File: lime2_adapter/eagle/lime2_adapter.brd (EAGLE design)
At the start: 23 parts, among them T1 MOSFET-N-NX7002AK, T2 MOSFET-N-NX7002AK, X1 lcd0_d02, X2 D-SUB15-HDR15RA, X4 XF2-40-RARBT, X5 FPC40-525594052

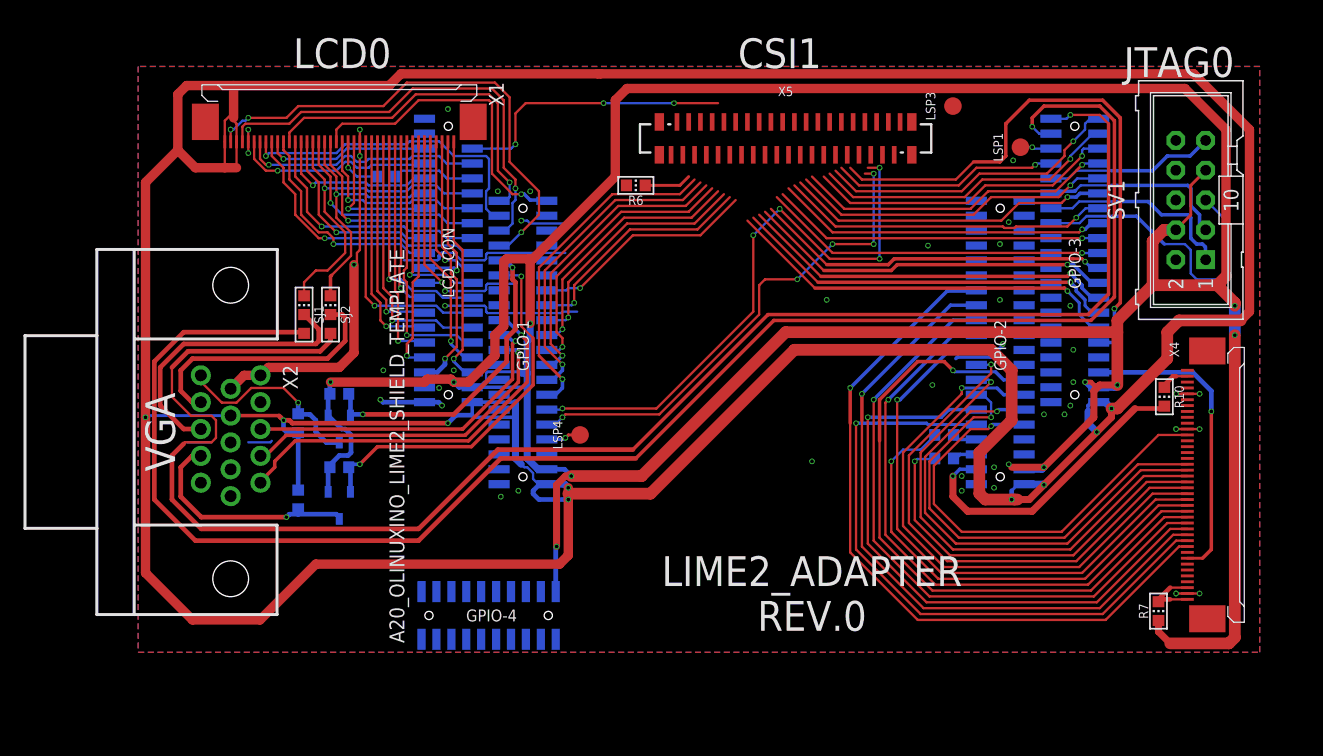
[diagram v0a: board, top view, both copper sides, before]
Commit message: Realize ECOs from Luc 190508
- Change X1-02 (X1B) to be disconnected
- Change X1-04 (X1D) to be disconnected
- Change X1-06 (X1F) to be disconnected
- Change X1-07 (X1G) to GPIO1-38(PC24)
- Change X1-08 (X1H) to GPIO1-40(PC23)
- Change X1-12 (X1L) to be disconnected
- Change X1-20 (X1T) to be disconnected
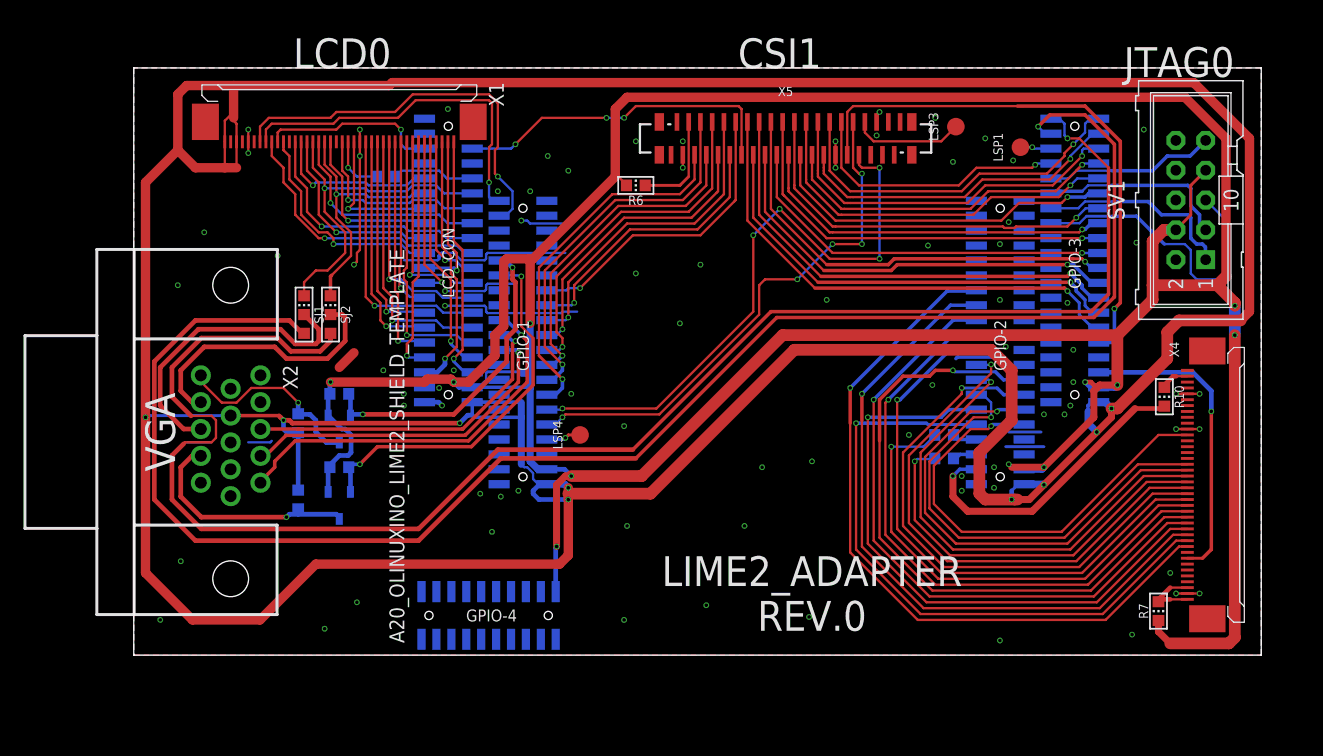
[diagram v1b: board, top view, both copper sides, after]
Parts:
- X1: value lcd0_d02 -> LCD
- moved LSP3 1.77 mm to (71.0, 51.0)
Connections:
- net EINT15/NCE7/SPI2_MISO/PC22: no longer X1.20
- net NC/IR0_RX/PB4: no longer X1.6
- net NC/IR0_TX/SPDIF_MCLK/STANBYWFI/PB3: no longer X1.7
- net NDQS/PC24: now also X1.7; no longer X1.8
- net SPI0_CS0/PC23: now also X1.8; no longer X1.12
- net TWI1_SCK/PB18: no longer X1.4
- net TWI1_SDA/PB19: no longer X1.2
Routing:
- net TWI1_SDA/PB19: track 42.5 -> 0.00 mm, vias 3 -> 0
- net TWI1_SCK/PB18: track 37.7 -> 0.00 mm, vias 1 -> 0
- net EINT15/NCE7/SPI2_MISO/PC22: track 27.1 -> 0.00 mm, vias 1 -> 0
- net NC/IR0_TX/SPDIF_MCLK/STANBYWFI/PB3: track 20.7 -> 0.00 mm, vias 1 -> 0
- net NC/IR0_RX/PB4: track 17.0 -> 0.00 mm, vias 1 -> 0
- net GND: track 90.0 -> 77.9 mm, vias 43 -> 82
- net DISPEN: track 0.00 -> 9.48 mm
- net CSI1_D9/PH9: track 34.3 -> 42.7 mm
- net CSI1_D11/PH11: track 32.2 -> 40.1 mm
- net CSI1_D13/PH13: track 30.4 -> 37.8 mm
- net NDQS/PC24: track 27.0 -> 34.1 mm
- net CSI1_D7/PG11: track 19.3 -> 25.9 mm
- net CSI1_D5/PG9: track 21.3 -> 27.4 mm
- net CSI1_D15/PH15: track 28.5 -> 34.6 mm
- net CSI1_D3/PG7: track 24.0 -> 29.7 mm
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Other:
- board outline added: 96 x 50 mm

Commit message: lime2_adapter
- Change VCC_CSI0 (Camera) from X4-2 to X4-3
- Connect X1-2 to GND.
- Provide access to TVOUT3, LINEIN[L|R] and FMIN[L|R]
- Provide access to MIC[1|2]
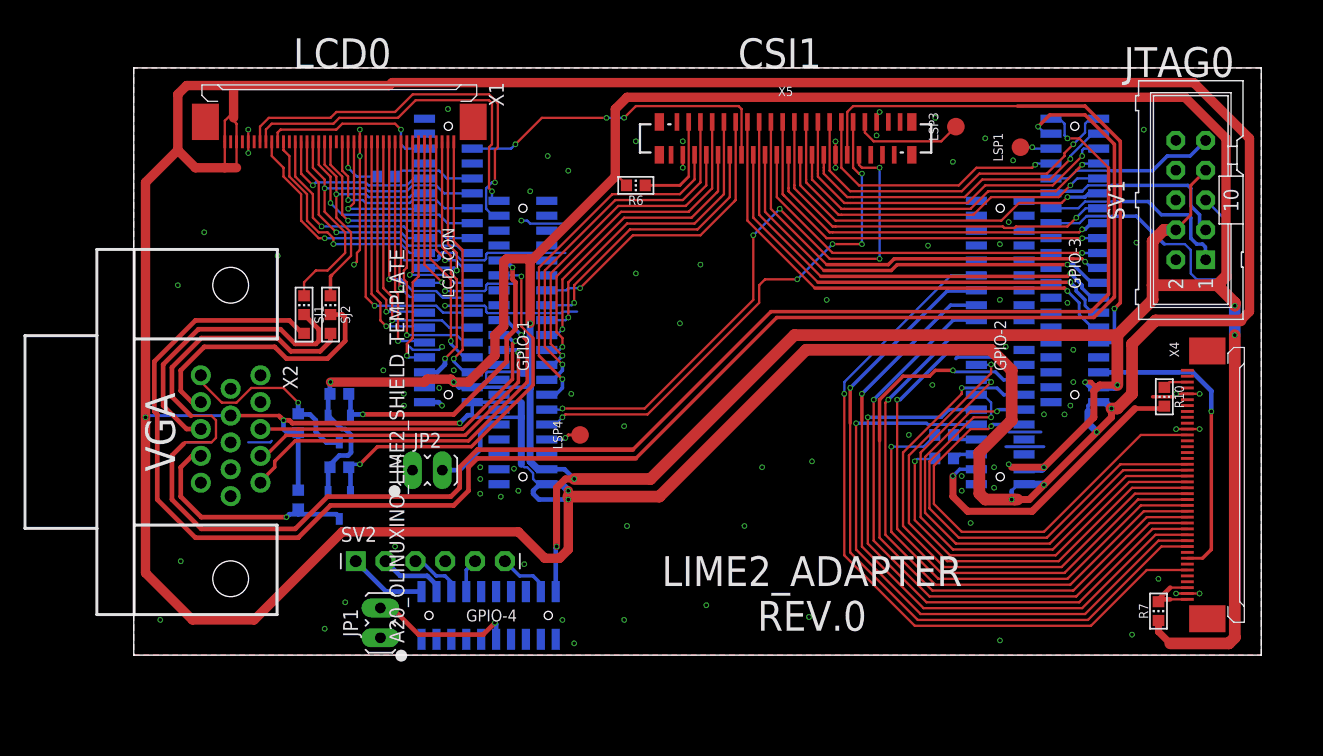
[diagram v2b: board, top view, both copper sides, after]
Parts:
- added JP1, JP2: JP1E, jumper:JP1
- added SV2: (no value), con-lstb:MA06-1
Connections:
- removed net CSI0_IO0: X4.35
- removed net GNDA: A20_OLINUXINO_LIME2_SHIELD.1-4
- removed net N$24: X4.16
- removed net N$25: X4.15
- removed net N$26: X4.14
- removed net N$27: X4.13
- removed net N$30: X4.10
- removed net N$31: X4.9
- removed net N$32: X4.8
- removed net N$33: X4.7
- removed net N$34: X4.6
- removed net N$36: X4.4
- removed net N$37: X4.3
- removed net N$39: X4.1
- removed net N$4: X4.36
- removed net N$6: X4.34
- removed net N$7: R10.1, X4.2
- removed net N$8: X4.32
- net FMINL: now also SV2.1
- net FMINR: now also SV2.2
- net GND: now also A20_OLINUXINO_LIME2_SHIELD.1-4, JP1.1, JP2.1, SV2.4
- net HSDA/UART7_RX/PS2_SDA0/PI21: now also X4.35
- net LINEINL: now also SV2.3
- net LINEINR: now also SV2.5
- net MICIN1: now also JP2.2
- net MICIN2: now also JP1.2
- net N$3: now also R10.1, X4.3; no longer X4.37
- net TVOUT3: now also SV2.6
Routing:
- net HSDA/UART7_RX/PS2_SDA0/PI21: track 0.00 -> 63.4 mm, vias 0 -> 1
- net MICIN2: track 0.00 -> 12.5 mm, vias 0 -> 1
- net MICIN1: track 0.00 -> 7.32 mm
- net FMINL: track 0.00 -> 6.67 mm
- net FMINR: track 0.00 -> 5.74 mm
- net LINEINL: track 0.00 -> 4.60 mm
- net TVOUT3: track 0.00 -> 4.53 mm
- net GND: track 77.9 -> 81.2 mm, vias 82 -> 89
- net LINEINR: track 0.00 -> 2.90 mm
- net +5V: track 369.4 -> 372.1 mm
- net N$7: track 2.47 -> 0.00 mm
- net N$3: track 0.00 -> 2.15 mm
- net LCD1_VSYNC/PH27: track 139.8 -> 140.8 mm
- net LCD1_HSYNC/PH26: track 141.1 -> 141.9 mm
- net CSI1_VSYNC/PG3: track 51.4 -> 50.8 mm
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
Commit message: lime2_adapter: Move LCD connector left to avoid collision with USB/ETH.
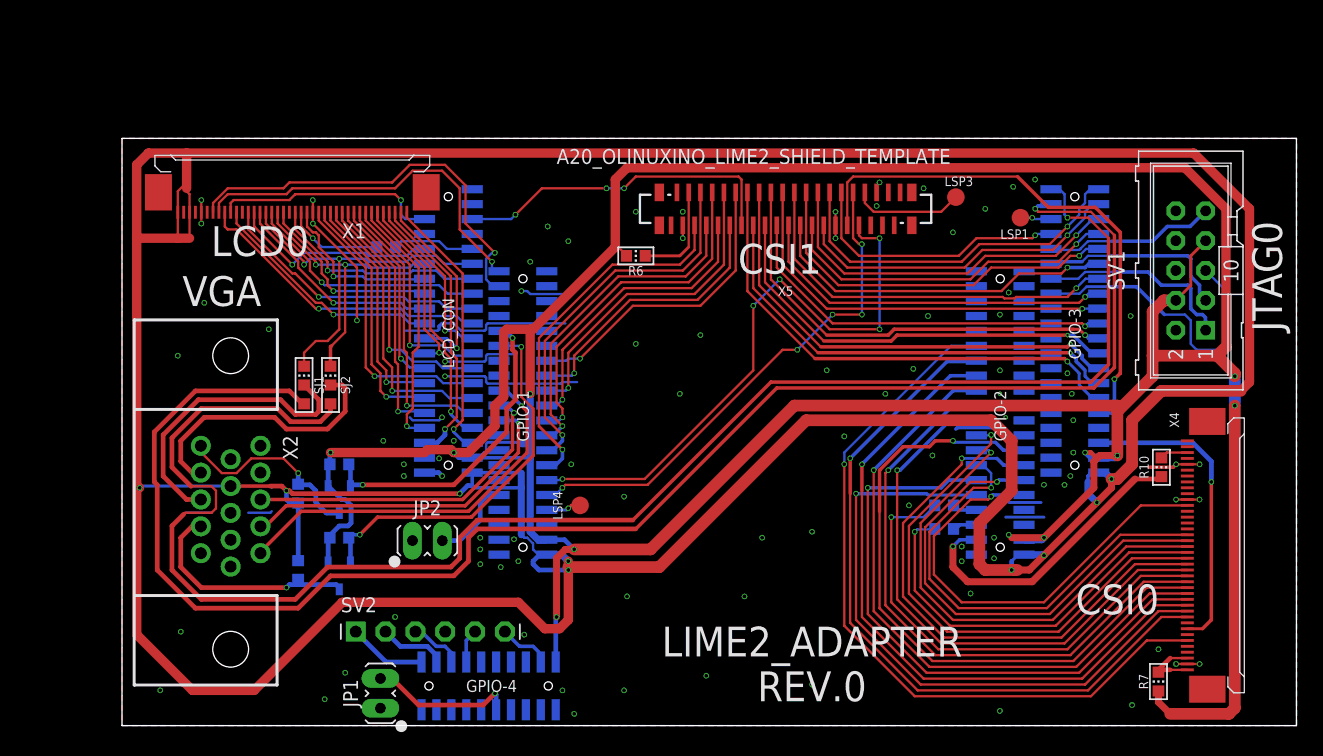
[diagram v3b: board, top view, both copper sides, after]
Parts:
- moved X1 7.21 mm to (14.5, 46.2)
- moved R10 6.01 mm to (88.5, 22.0)
- moved A20_OLINUXINO_LIME2_SHIELD 6.00 mm to (54.5, 26.4)
- moved JP1 6.00 mm to (22.0, 2.75)
- moved JP2 6.00 mm to (26.0, 15.8)
- moved LSP1 6.00 mm to (76.5, 43.2)
- moved LSP3 6.00 mm to (71.0, 45.0)
- moved LSP4 6.00 mm to (39.0, 18.8)
- moved R1 6.00 mm to (22.5, 40.8)
- moved R2 6.00 mm to (18.5, 16.0)
- moved R3 6.00 mm to (15.0, 13.2)
- moved R4 6.00 mm to (18.5, 22.2)
- moved R5 6.00 mm to (15.0, 19.8)
- moved R6 6.00 mm to (43.8, 40.0)
- moved R7 6.00 mm to (88.2, 3.75)
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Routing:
- net PWM0: track 15.2 -> 19.2 mm
- net LCD0_DE: track 14.1 -> 17.8 mm
- net LCD0_CLKR: track 4.97 -> 8.38 mm
- net LCD0_D06: track 16.2 -> 18.9 mm
- net LCD0_D15: track 14.1 -> 16.6 mm
- net LCD0_D04: track 18.4 -> 20.9 mm
- net LCD0_HSYNC: track 29.4 -> 31.9 mm, vias 1 -> 2
- net LCD0_D05: track 13.9 -> 16.3 mm
- net LCD0_D00: track 23.6 -> 25.8 mm
- net N$4: track 0.00 -> 2.05 mm
- net LCD0_D07: track 12.5 -> 14.4 mm
- net LCD0_VSYNC: track 22.5 -> 24.5 mm, vias 1 -> 2
- net LCD0_D02: track 21.4 -> 23.3 mm
- net LCD1_HSYNC/PH26: track 141.9 -> 140.1 mm
- net LCD0_D03: track 16.5 -> 18.3 mm
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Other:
- board size 96 x 50 mm -> 100 x 50 mm
- board text added: "CSI0"
- board text removed: "FIXME: - Check VGA connector"
